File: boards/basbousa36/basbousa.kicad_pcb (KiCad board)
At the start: 2 copper layers, 133.4 x 90.7 mm, 26 parts

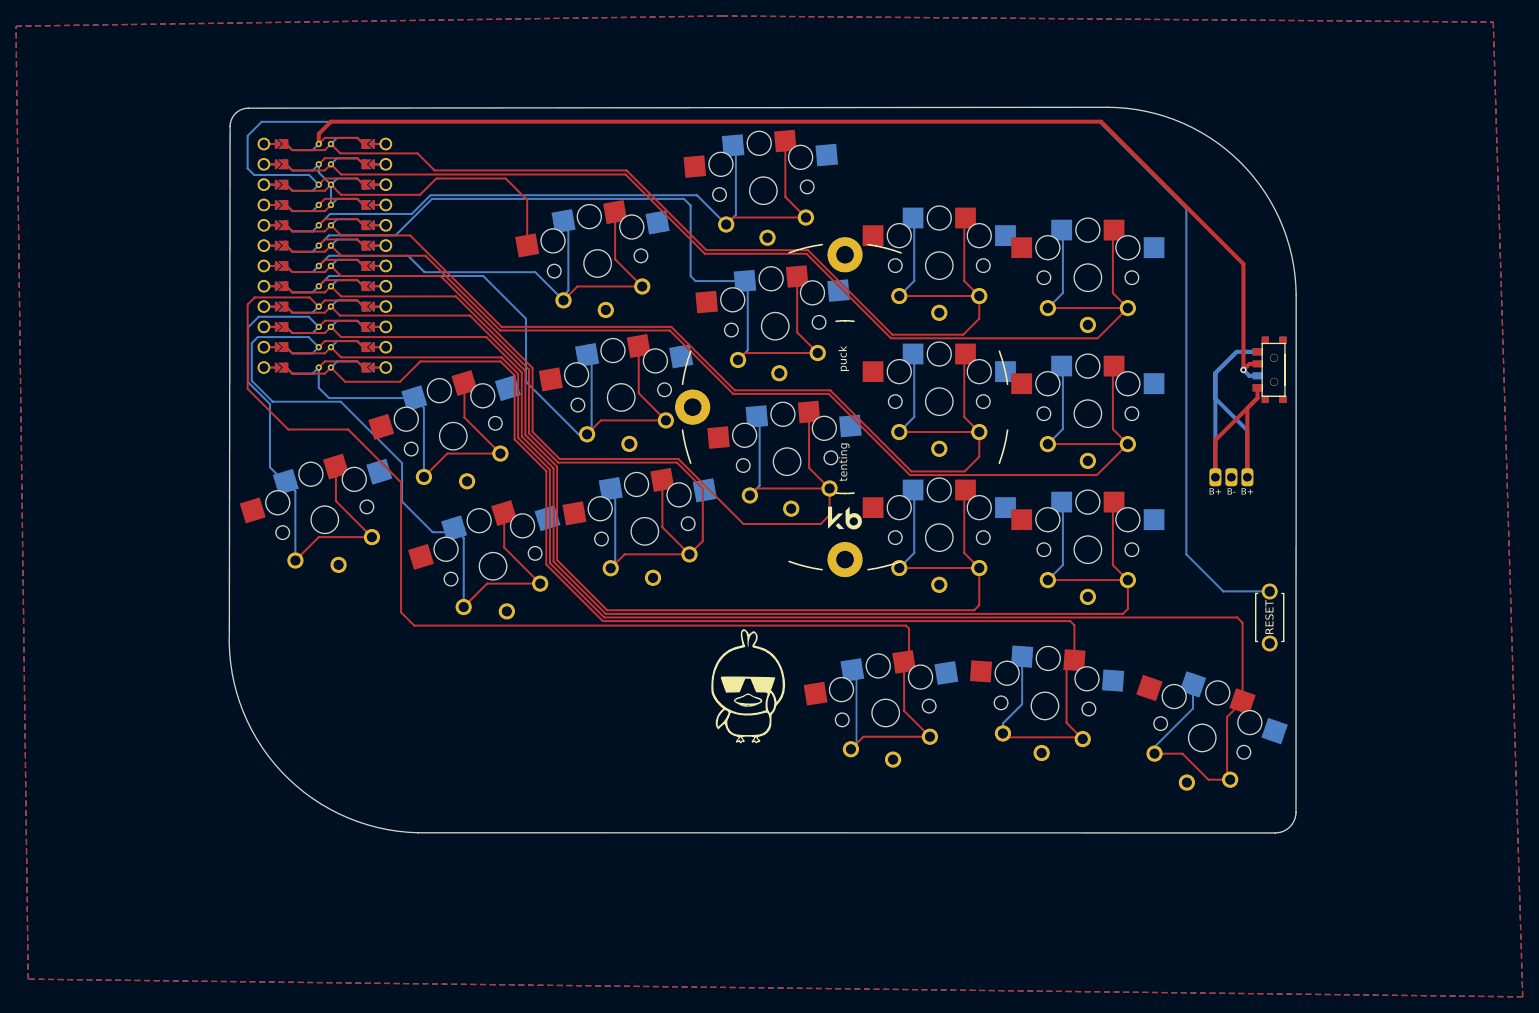
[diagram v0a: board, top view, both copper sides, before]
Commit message: basbousa new case with holes and chocV2 change
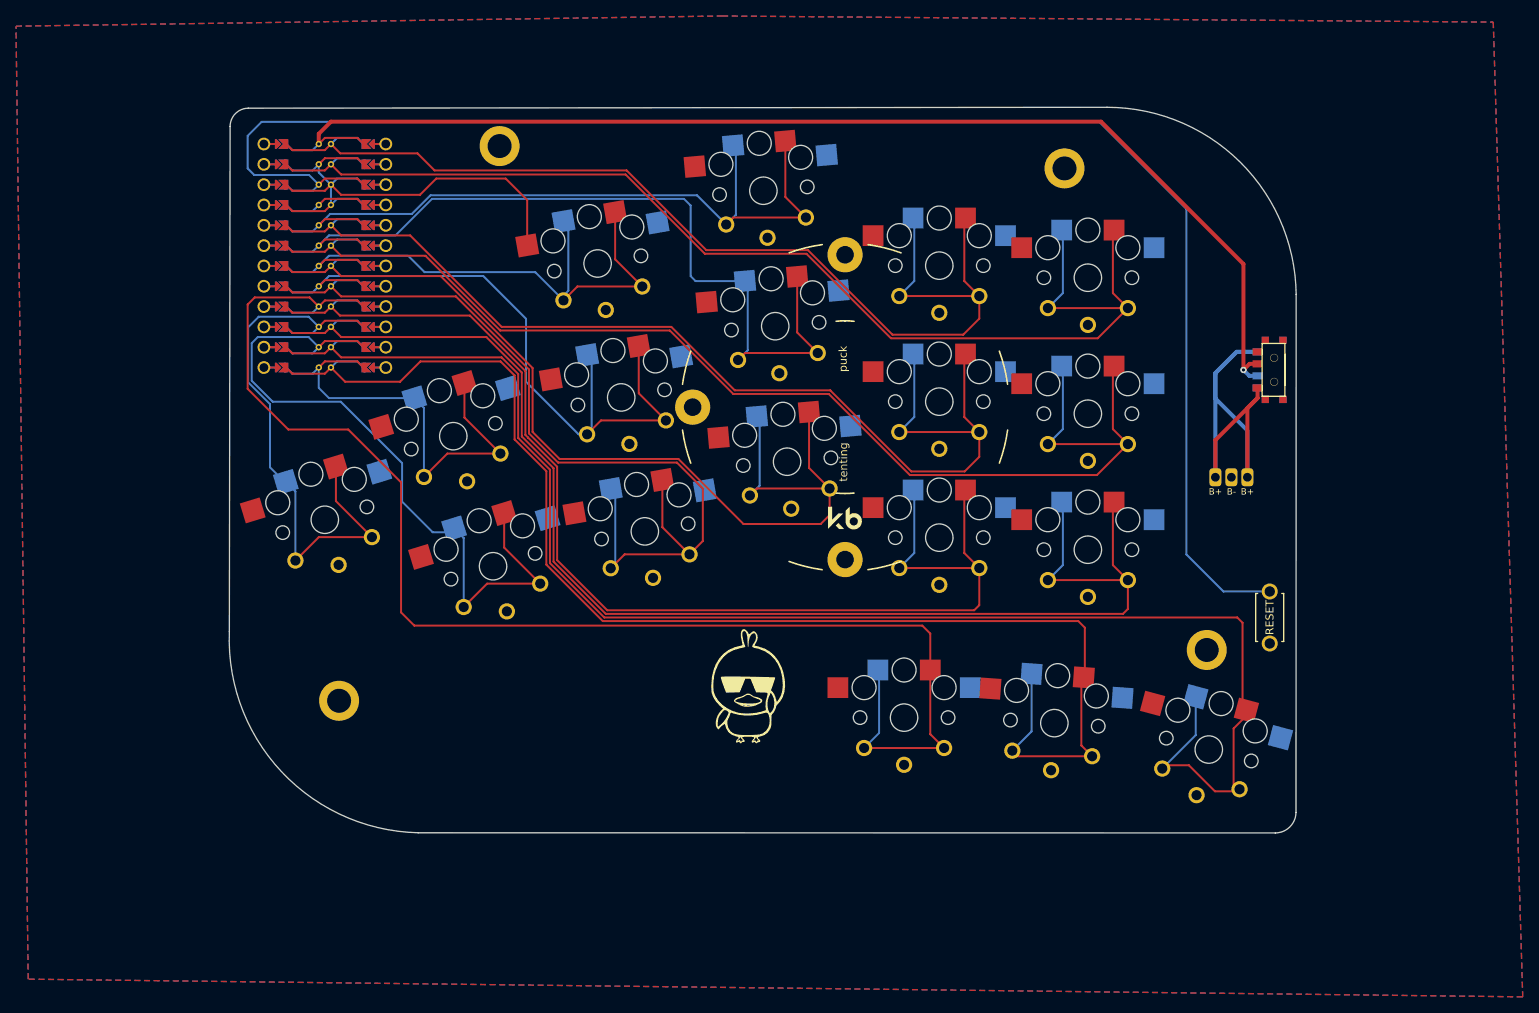
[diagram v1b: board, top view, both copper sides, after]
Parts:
- added ?: , , F.Cu at (60.5, -119.6)
- added ?: , , F.Cu at (40.4, -50.3)
- added ?: , , F.Cu at (131.1, -116.8)
- added ?: , , F.Cu at (148.8, -56.6)
- moved S31 2.45 mm to (129.8, -47.5)
- moved S31 2.37 mm to (111.0, -48.2), turned to 0 degrees
- moved S33 1.67 mm to (149.1, -44.2), turned to -15 degrees
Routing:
- net P15: track 160.1 -> 163.4 mm
- net P9: track 156.2 -> 159.0 mm
